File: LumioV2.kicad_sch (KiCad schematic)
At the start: 56 parts, among them J1 I2C POINT 1 - QWIIC, J10 MOTOR B, J11 Analog Input, J12 Analog Input, J13 Analog Input, J14 Analog Input, J15 Analog Input, J16 Analog Input, J17 Analog Input, J18 Analog Input, J2 I2C POINT 2 - QWIIC, J3 I2C POINT 3 - JST-PH, J4 I2C POINT 4 - JST-PH, J5 Raspi 5, J6 US Dist - Front, J7 US Dist - Back, J8 Display Connector, J9 MOTOR A, U1 LM2577T-ADJ/NOPB, U2 L298N, U3 MCP3008

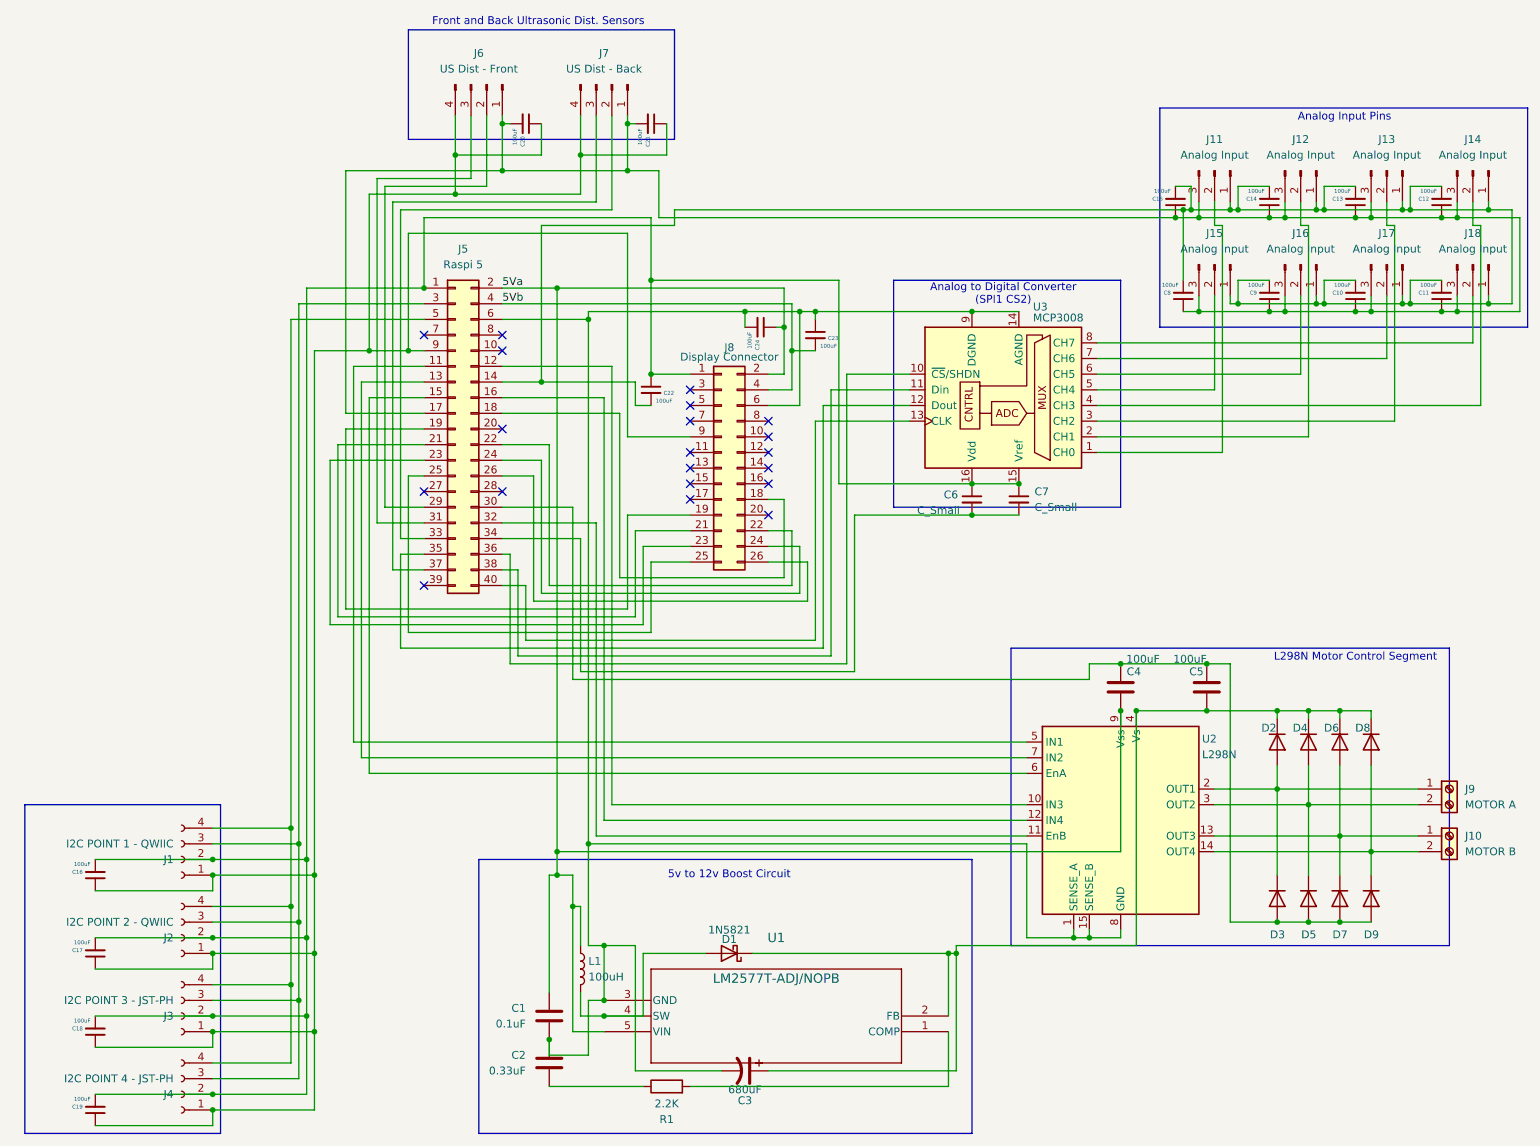
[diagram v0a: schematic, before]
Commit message: correcrted pin orde rin schematics and added most footprints
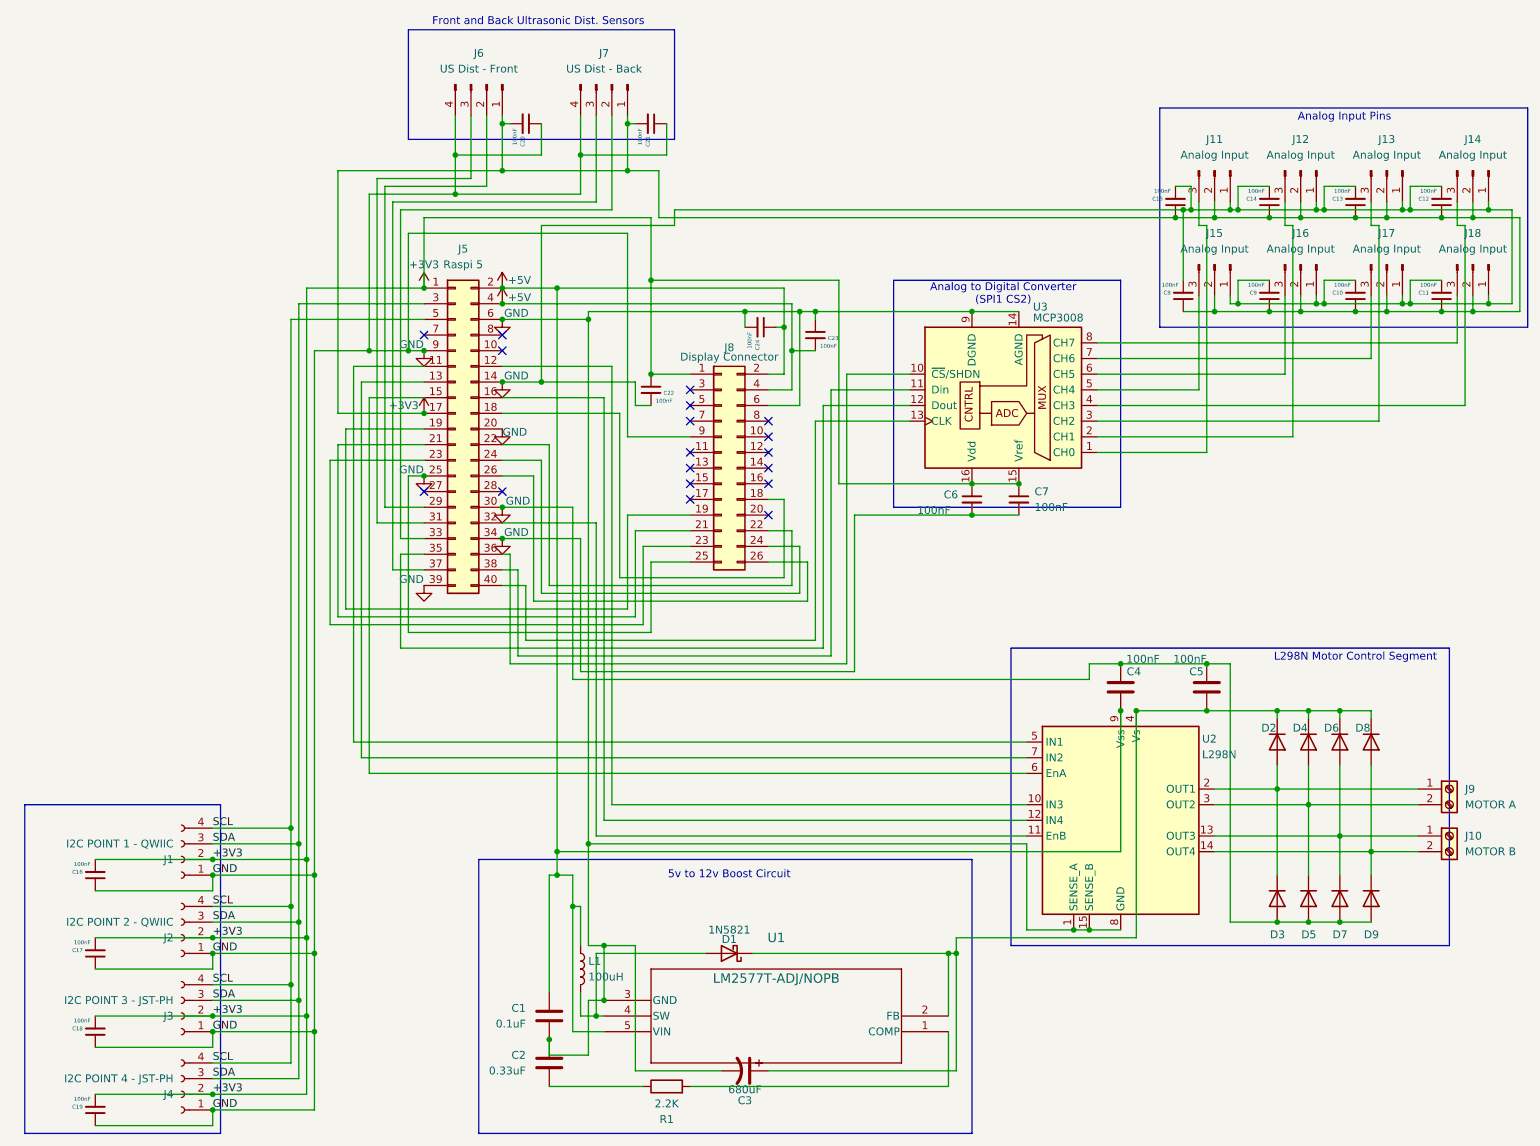
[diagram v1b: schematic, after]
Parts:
- C1, C2: footprint (none) -> Capacitor_SMD:C_0603_1608Metric
- C10, C11, C12, C13, C14, C15, C16, C17, C18, C19, C20, C21, C22, C23, C24, C4, C5, C8, C9: value 100uF -> 100nF; footprint (none) -> Capacitor_SMD:C_0603_1608Metric
- C3: footprint (none) -> Capacitor_SMD:CP_Elec_10x10
- C6, C7: value C_Small -> 100nF; footprint (none) -> Capacitor_SMD:C_0603_1608Metric
- U3: footprint (none) -> Package_SO:SOIC-16_3.9x9.9mm_P1.27mm
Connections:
- net 5Vb is gone; now on net +5V: C23.2, J5.4 (5V), J8.4 (Pin_4)
- net GND: now reaches C16.1, C17.1, C18.1, C19.1, C20.1, C21.1, J1.1 (Pin_1), J2.1 (Pin_1), J3.1 (Pin_1), J4.1 (Pin_1), J5.9 (GND), J6.4 (Pin_4), J7.4 (Pin_4), J8.9 (Pin_9)
- net GND: now also C1.2, C10.2, C11.2, C12.2, C13.2, C14.2, C15.2, C2.1, C22.2, C23.1, C24.2, C3.2, C4.1, C5.1, C6.2, C7.2, C8.2, C9.2, D3.2 (A), D5.2 (A), D7.2 (A), D9.2 (A), J11.1 (Pin_1), J12.1 (Pin_1), J13.1 (Pin_1), J14.1 (Pin_1), J15.1 (Pin_1), J16.1 (Pin_1), J17.1 (Pin_1), J18.1 (Pin_1), J5.14 (GND), J5.20 (GND), J5.25 (GND), J5.30 (GND), J5.34 (GND), J5.39 (GND), J5.6 (GND), J8.25 (Pin_25), J8.6 (Pin_6), U1.3 (GND), U2.1 (SENSE_A), U2.15 (SENSE_B), U2.8 (GND), U3.14 (AGND), U3.9 (DGND)
- net +3V3: now reaches C16.2, C17.2, C18.2, C19.2, C22.1, C6.1, C7.1, J1.2 (Pin_2), J2.2 (Pin_2), J3.2 (Pin_2), J4.2 (Pin_2), J5.1 (Pin_1), J8.1 (Pin_1), U3.15 (Vref), U3.16 (Vdd)
- net +3V3: now also C10.1, C11.1, C12.1, C13.1, C14.1, C15.1, C20.2, C21.2, C8.1, C9.1, J11.2 (Pin_2), J12.2 (Pin_2), J13.2 (Pin_2), J14.2 (Pin_2), J15.2 (Pin_2), J16.2 (Pin_2), J17.2 (Pin_2), J18.2 (Pin_2), J5.17 (3V3), J6.1 (Pin_1), J7.1 (Pin_1)
- net SDA: now reaches J1.3 (Pin_3), J2.3 (Pin_3), J3.3 (Pin_3), J4.3 (Pin_3), J5.3 (SDA1)
- net SCL: now reaches J1.4 (Pin_4), J2.4 (Pin_4), J3.4 (Pin_4), J4.4 (Pin_4), J5.5 (Pin_5)
- net at U3.1 (CH0): now also J11.3 (Pin_3); no longer J11.2 (Pin_2)
- net at U3.2 (CH1): now also J12.3 (Pin_3); no longer J12.2 (Pin_2)
- net at U3.3 (CH2): now also J13.3 (Pin_3); no longer J13.2 (Pin_2)
- net at U3.4 (CH3): now also J14.3 (Pin_3); no longer J14.2 (Pin_2)
- net at U3.5 (CH4): now also J15.3 (Pin_3); no longer J15.2 (Pin_2)
- net at U3.6 (CH5): now also J16.3 (Pin_3); no longer J16.2 (Pin_2)
- net at U3.7 (CH6): now also J17.3 (Pin_3); no longer J17.2 (Pin_2)
- net at U3.8 (CH7): now also J18.3 (Pin_3); no longer J18.2 (Pin_2)
- net 5Va renamed +5V
- no-connect marks 20 -> 18
